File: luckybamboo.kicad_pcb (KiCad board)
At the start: 4 copper layers, 70.7 x 53.3 mm, 153 parts, among them J1 NEIGHBOR1, J10 TEST_2P, J11 TEST_2P, J12 TEST_2P, J13 TEST_2P, J14 TEST_2P, J15 TEST_2P, J16 TEST_2P, J17 Conn_Coaxial, J18 Conn_Coaxial, J19 TEST_2P, J2 NEIGHBOR2, J20 TEST_2P, J21 TEST_2P, J22 TEST_2P, J23 TEST_2P, J24 TEST_2P, J25 TEST_2P, J26 TEST_2P, J27 TEST_2P, J28 TEST_2P, J29 TEST_2P, J3 Conn_01x08, J30 TEST_2P, J31 TEST_2P, J32 TEST_2P, J33 TEST_2P, J4 Conn_01x08, J5 Conn_01x08, J6 Conn_01x08, J7 BONUS_ROW, J8 TEST_2P, J9 TEST_2P, U1 ADF7242, U10 ADF7242_balun, U11 ADF7242_balun, U12 HHM2293A1, U13 BGA7H1N6, U14 ADF7242_balun, U15 ADF7242_balun, U16 ADF7242_balun, U17 ADF7242_balun, U2 ADF7242, U3 ADF7242, U4 ADF7242, U5 SKY13322, U6 HHM2293A1, U7 HHM2293A1, U8 ADF7242_balun, U9 ADF7242_balun, X1 XTAL4PIN, X2 XTAL4PIN, X3 XTAL4PIN, X4 XTAL4PIN

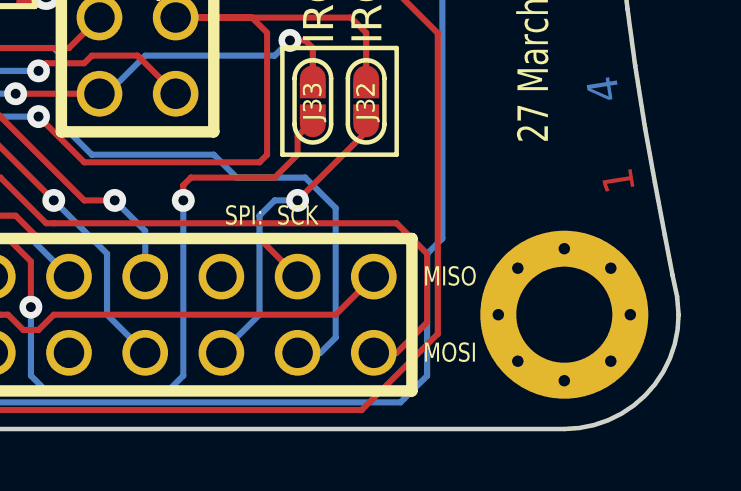
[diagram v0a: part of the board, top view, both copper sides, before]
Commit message: adopt OSHWA convention for SPI signal names https://www.oshwa.org/a-resolution-to-redefine-spi-signal-names
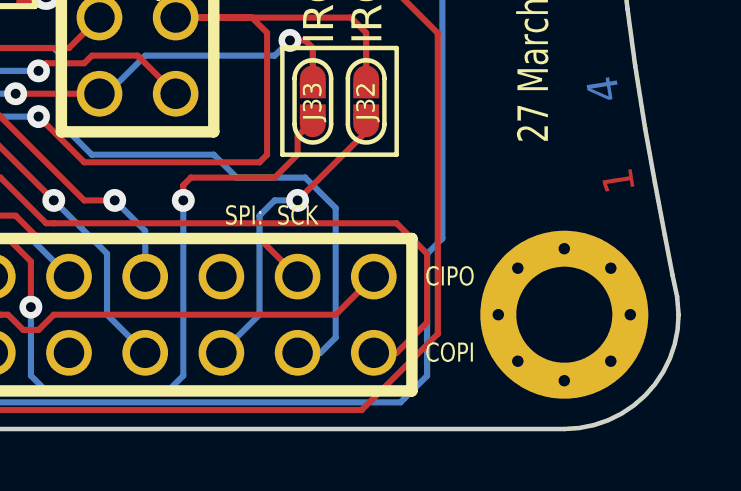
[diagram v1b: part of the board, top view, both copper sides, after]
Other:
- board text added: "CIPO"
- board text added: "COPI"
- board text removed: "MISO"
- board text removed: "MOSI"
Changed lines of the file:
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@@
     (effects (font (size 0.635 0.508) (thickness 0.1016)))
   )
-  (gr_text MISO (at 172.72 116.84) (layer F.SilkS)
+  (gr_text CIPO (at 172.72 116.84) (layer F.SilkS)
     (effects (font (size 0.635 0.508) (thickness 0.1016)))
   )
-  (gr_text MOSI (at 172.72 119.38) (layer F.SilkS)
+  (gr_text COPI (at 172.72 119.38) (layer F.SilkS)
     (effects (font (size 0.635 0.508) (thickness 0.1016)))
   )
